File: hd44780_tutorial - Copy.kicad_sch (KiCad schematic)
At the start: 30 parts, among them J1 LCD_2004_PinSocket_1x16_P2.54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, J2 UJC-HP-3-SMT-TR, SW1 REG SELECT, SW2 ENABLE, SW3 DS02C-254-1L-08BE

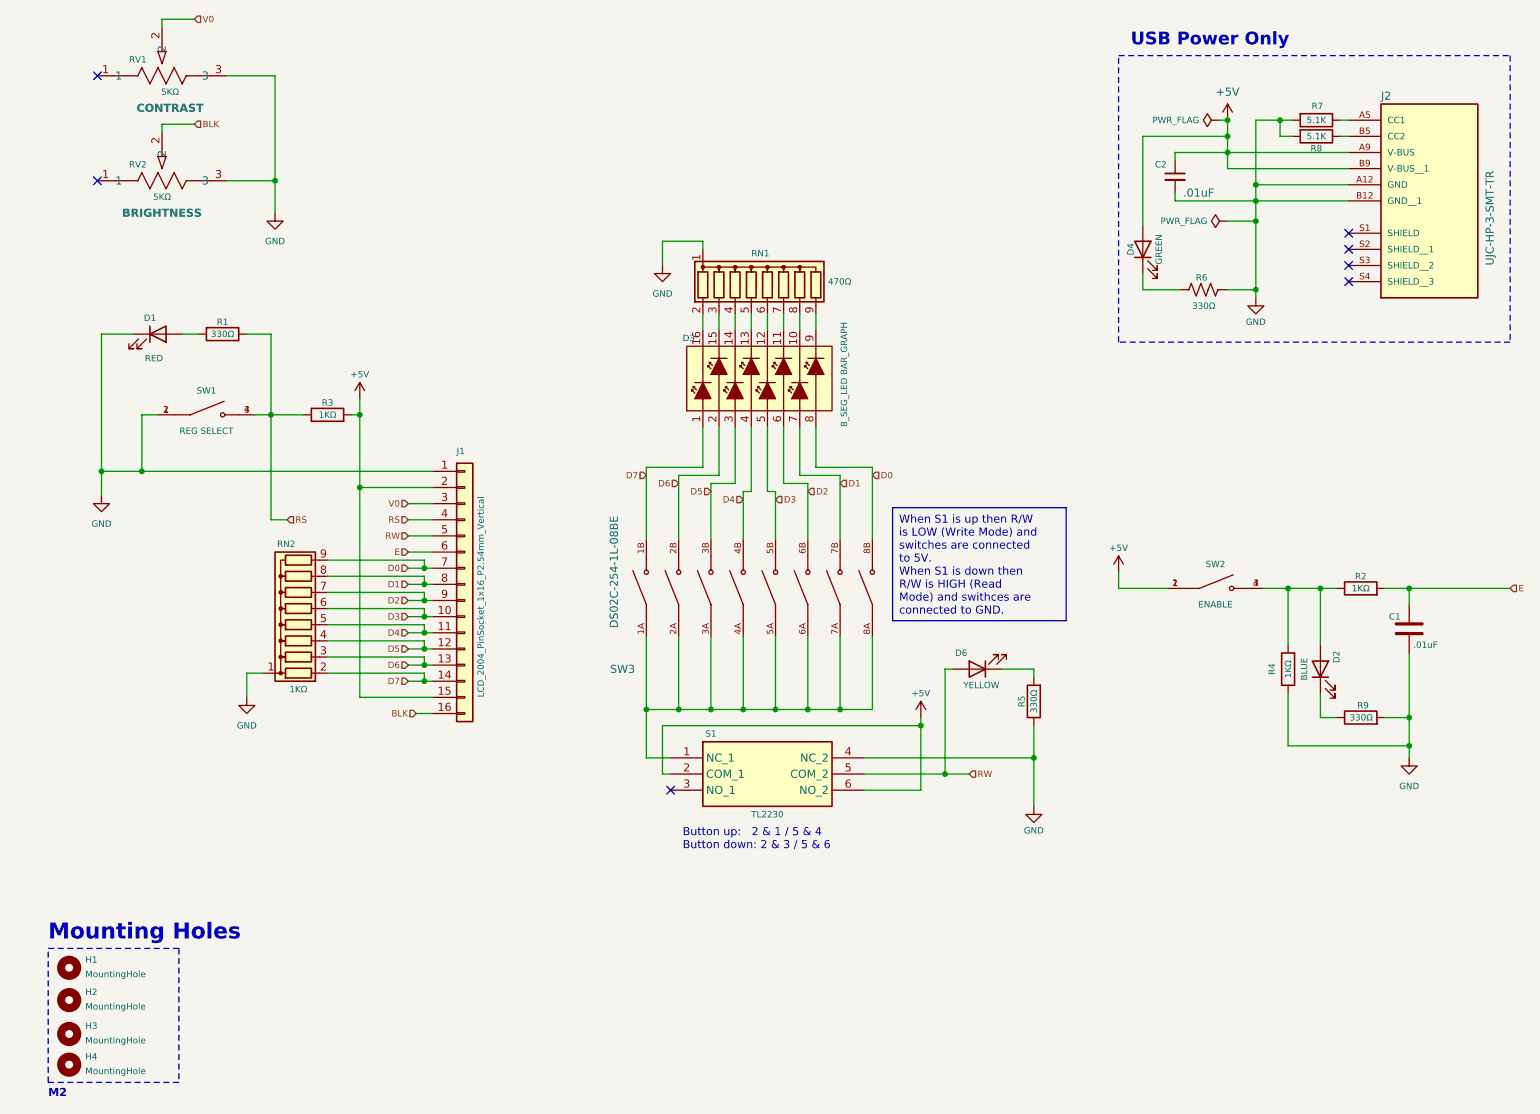
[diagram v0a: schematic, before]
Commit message: Determined that adding 1K resistor to SW2 fixes the problem with this board. Created new gerber/drill files.
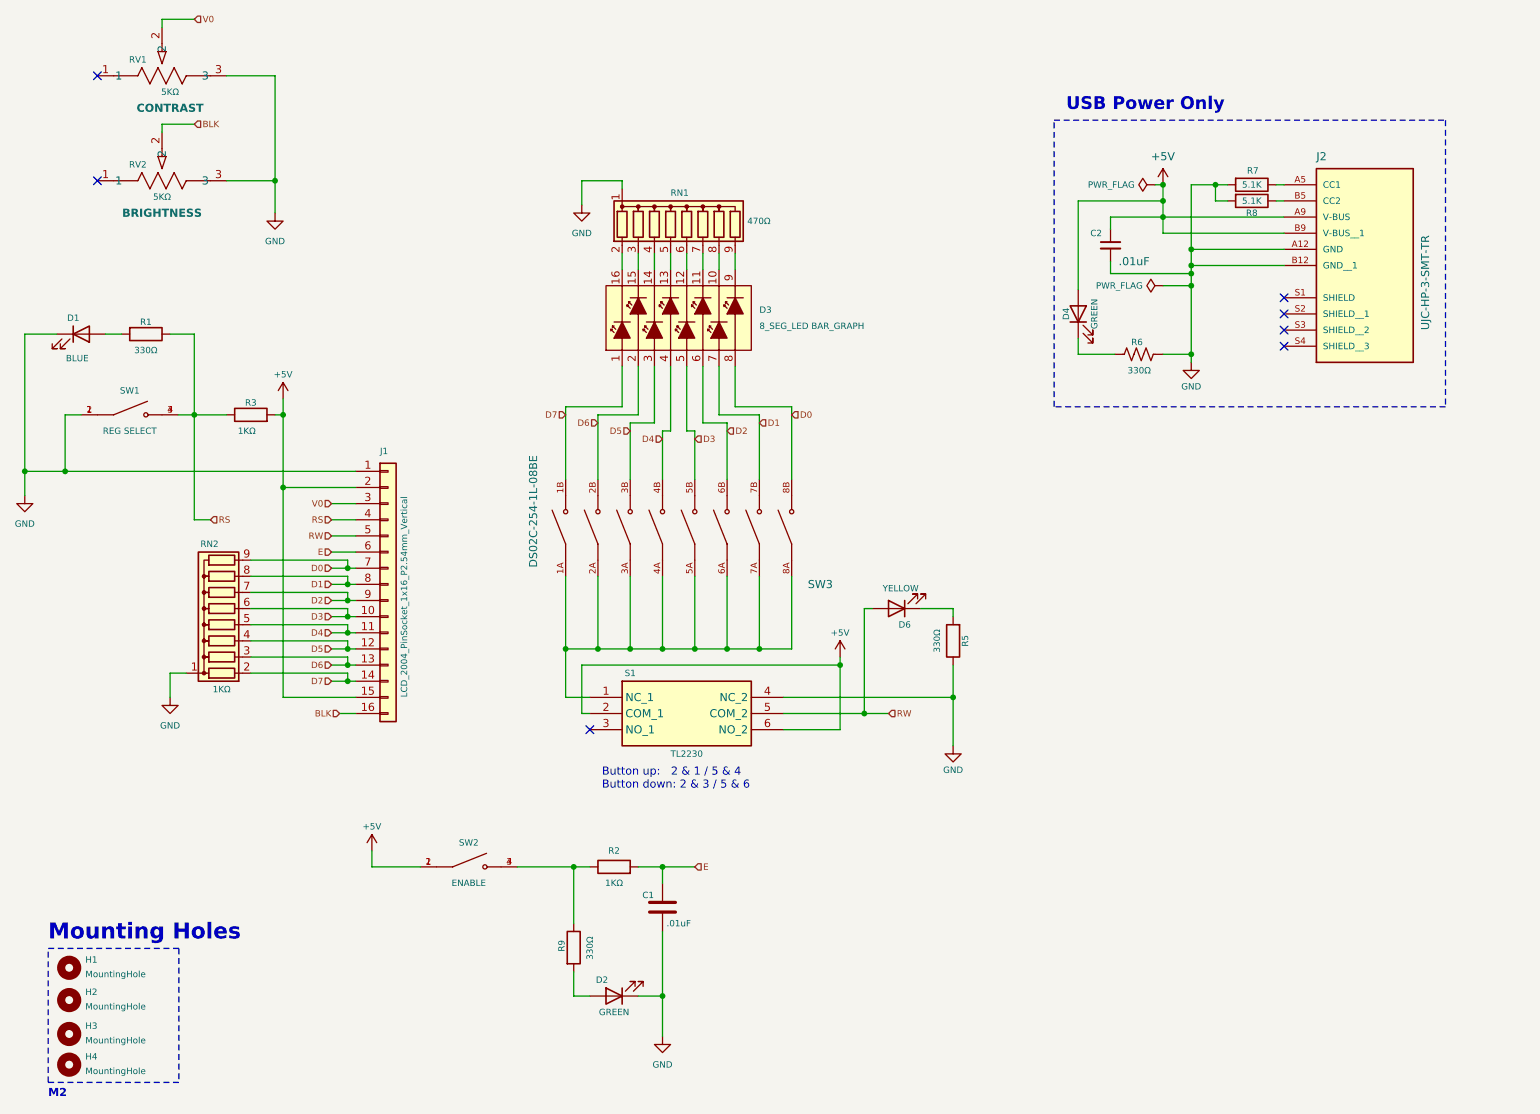
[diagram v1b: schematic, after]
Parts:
- removed R4: 1KΩ, Resistor_THT:R_Axial_DIN0207_L6.3mm_D2.5mm_P7.62mm_Horizontal, symbol Device:R
- C2: footprint Capacitor_THT:C_Disc_D4.7mm_W2.5mm_P5.00mm -> (none)
- D1: value RED -> BLUE
- D2: value BLUE -> GREEN
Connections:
- net GND: now also D2.1 (K); no longer R9.2
- net at R2.1, SW2.3, SW2.4: now also R9.1; no longer D2.2 (A)
- new net: D2.2 (A), R9.2
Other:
- moved on the sheet: C1, C2, D1, D3, D4, D6, J1, J2, R1, R2, R3, R5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
